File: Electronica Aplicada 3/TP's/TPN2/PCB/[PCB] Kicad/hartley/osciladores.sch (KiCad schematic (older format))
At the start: 16 parts, among them J1 Conn_01x01_Female, J2 Conn_01x01_Female, J3 Conn_01x01_Female, J4 Conn_01x01_Female, Q1 2N3904

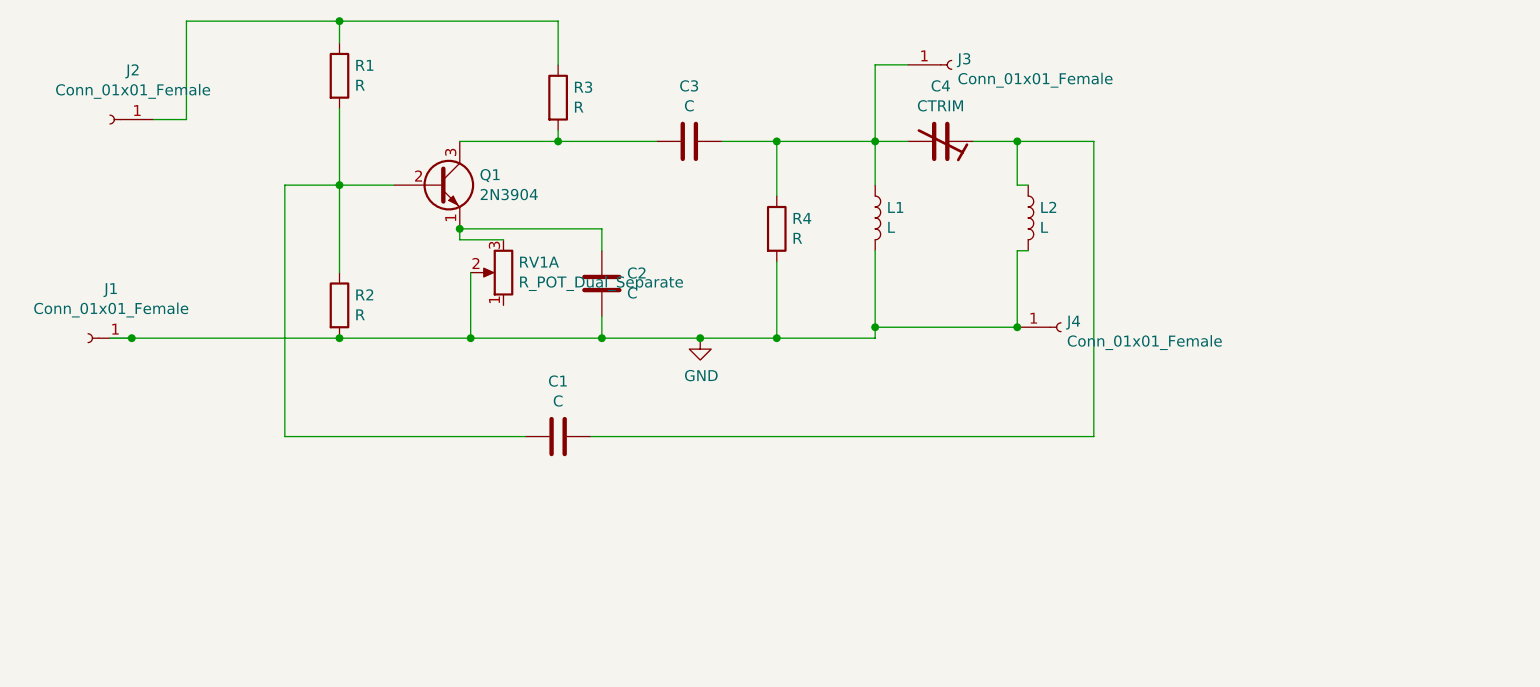
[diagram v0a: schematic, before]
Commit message: Agrego rediseño de Hartley (kicad)
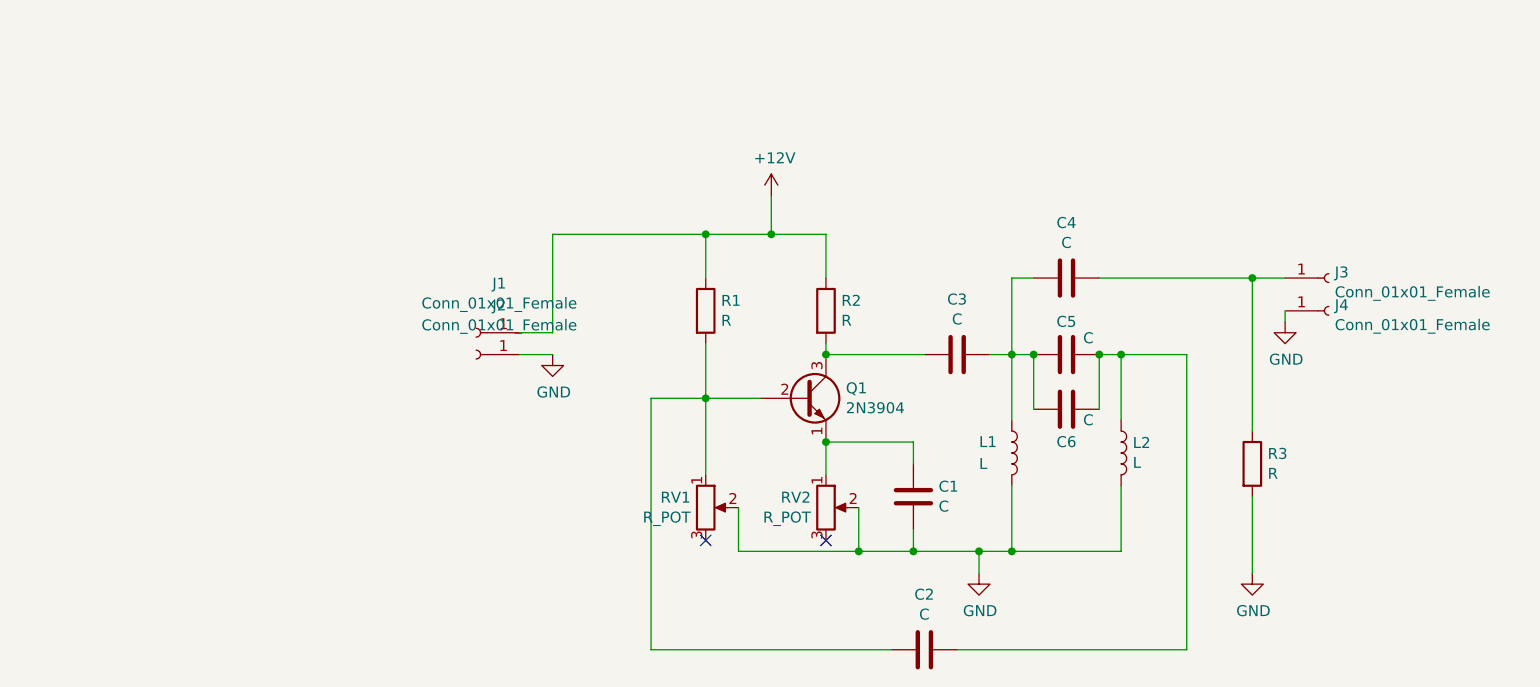
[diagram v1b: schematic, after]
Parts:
- removed C4: CTRIM, Potentiometers:Potentiometer_Trimmer_Bourns_3339P_Horizontal, symbol Device:CTRIM
- removed R2, R4: R, Resistors_THT:R_Box_L13.0mm_W4.0mm_P9.00mm, symbol Device:R
- removed RV1: R_POT_Dual_Separate, Potentiometers:Potentiometer_Trimmer_ACP_CA14h2.5_Vertical_Px2.5mm_Py10.0mm, symbol Device:R_POT_Dual_Separate
- added C4, C5, C6: C, Capacitor_THT:C_Disc_D7.5mm_W2.5mm_P5.00mm, symbol Device:C
- added R3: R, Resistor_THT:R_Axial_DIN0207_L6.3mm_D2.5mm_P10.16mm_Horizontal, symbol Device:R
- added RV1, RV2: R_POT, Potentiometer_THT:Potentiometer_Alps_RK163_Single_Horizontal, symbol Device:R_POT
- C1: renamed from C2; footprint Capacitors_THT:CP_Radial_Tantal_D4.5mm_P5.00mm -> Capacitor_THT:C_Disc_D5.0mm_W2.5mm_P5.00mm
- C2: renamed from C1; footprint Capacitors_THT:CP_Radial_D4.0mm_P2.00mm -> Capacitor_THT:C_Disc_D7.5mm_W2.5mm_P5.00mm
- C3: footprint Capacitors_THT:CP_Radial_Tantal_D4.5mm_P5.00mm -> Capacitor_THT:C_Disc_D7.5mm_W2.5mm_P5.00mm
- J1: renamed from J2; footprint Connectors:1pin -> Connector_PinHeader_2.54mm:PinHeader_1x01_P2.54mm_Horizontal
- J2: renamed from J1; footprint Connectors:1pin -> Connector_PinHeader_2.54mm:PinHeader_1x01_P2.54mm_Horizontal
- J3, J4: footprint Connectors:1pin -> Connector_PinHeader_2.54mm:PinHeader_1x01_P2.54mm_Horizontal
- L1, L2: footprint Inductors_THT:L_Axial_L12.0mm_D5.0mm_P15.24mm_Horizontal_Fastron_MISC -> Inductor_THT:L_Axial_L16.0mm_D6.3mm_P20.32mm_Horizontal_Fastron_VHBCC
- Q1: footprint TO_SOT_Packages_THT:TO-92_Rugged -> Package_TO_SOT_THT:TO-92_Inline_Horizontal2
- R1: footprint Resistors_THT:R_Box_L13.0mm_W4.0mm_P9.00mm -> Resistor_THT:R_Axial_DIN0207_L6.3mm_D2.5mm_P10.16mm_Horizontal
- R2: renamed from R3; footprint Resistors_THT:R_Box_L13.0mm_W4.0mm_P9.00mm -> Resistor_THT:R_Axial_DIN0207_L6.3mm_D2.5mm_P10.16mm_Horizontal
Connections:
- net GND: now also R3.2, RV1.2, RV2.2
- net +12V: now reaches J1.1 (Pin_1), R1.1, R2.1
- net at C2.2, Q1.2 (B), R1.2: now also RV1.1
- net at C1.1, Q1.1 (E): now also RV2.1
- net at C3.1, L1.1: now also C4.2, C5.2, C6.2; no longer J3.1 (Pin_1)
- net at C2.1, L2.1: now also C5.1, C6.1
- new net: C4.1, J3.1 (Pin_1), R3.1
- no-connect marks 0 -> 2
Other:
- moved on the sheet: C1, C2, C3, J1, J2, J3, J4, L1, L2, Q1, R1, R2

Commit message: Actualizo repo
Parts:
- removed RV1, RV2: R_POT, Potentiometer_THT:Potentiometer_Alps_RK163_Single_Horizontal, symbol Device:R_POT
- added R? (x2): R, Resistor_THT:R_Axial_DIN0207_L6.3mm_D2.5mm_P10.16mm_Horizontal, symbol Device:R
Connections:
- no-connect marks 2 -> 0
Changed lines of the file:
@@
 	1    0    0    -1
 $EndComp
-NoConn ~ 4975 4025
 $Comp
 L Connector:Conn_01x01_Female J3
@@
 Wire Wire Line
 	5925 4075 6225 4075
-$Comp
-L Device:R_POT RV1
-U 1 1 5CD676F6
-P 4975 3875
-F 0 "RV1" H 4906 3921 50  0000 R CNN
-F 1 "R_POT" H 4906 3830 50  0000 R CNN
-F 2 "Potentiometer_THT:Potentiometer_Alps_RK163_Single_Horizontal" H 4975 3875 50  0001 C CNN
-F 3 "~" H 4975 3875 50  0001 C CNN
-	1    4975 3875
-	1    0    0    -1
-$EndComp
 Wire Wire Line
 	4975 3725 4975 3375
 Wire Wire Line
-	5125 3875 5125 4075
-$Comp
-L Device:R_POT RV2
-U 1 1 5CD6A114
-P 5525 3875
-F 0 "RV2" H 5456 3921 50  0000 R CNN
-F 1 "R_POT" H 5456 3830 50  0000 R CNN
-F 2 "Potentiometer_THT:Potentiometer_Alps_RK163_Single_Horizontal" H 5525 3875 50  0001 C CNN
-F 3 "~" H 5525 3875 50  0001 C CNN
-	1    5525 3875
-	1    0    0    -1
-$EndComp
-Wire Wire Line
-	5125 4075 5675 4075
-Wire Wire Line
 	5525 3725 5525 3575
 Connection ~ 5525 3575
-Wire Wire Line
-	5675 3875 5675 4075
-Connection ~ 5675 4075
-Wire Wire Line
-	5675 4075 5925 4075
 $Comp
 L Device:C C4
@@
 Wire Wire Line
 	5275 2625 5525 2625
-NoConn ~ 5525 4025
+$Comp
+L Device:R R?
+U 1 1 5CDBE2EA
+P 4975 3900
+F 0 "R?" H 5045 3946 50  0000 L CNN
+F 1 "R" H 5045 3855 50  0000 L CNN
+F 2 "Resistor_THT:R_Axial_DIN0207_L6.3mm_D2.5mm_P10.16mm_Horizontal" V 4905 3900 50  0001 C CNN
+F 3 "~" H 4975 3900 50  0001 C CNN
+	1    4975 3900
+	1    0    0    -1
+$EndComp
+$Comp
+L Device:R R?
+U 1 1 5CDBEAEB
+P 5525 3900
+F 0 "R?" H 5595 3946 50  0000 L CNN
+F 1 "R" H 5595 3855 50  0000 L CNN
+F 2 "Resistor_THT:R_Axial_DIN0207_L6.3mm_D2.5mm_P10.16mm_Horizontal" V 5455 3900 50  0001 C CNN
+F 3 "~" H 5525 3900 50  0001 C CNN
+	1    5525 3900
+	1    0    0    -1
+$EndComp
+Wire Wire Line
+	4975 4050 4975 4075
+Wire Wire Line
+	4975 4075 5525 4075
+Wire Wire Line
+	5525 4050 5525 4075
+Connection ~ 5525 4075
+Wire Wire Line
+	5525 4075 5925 4075
 $EndSCHEMATC
